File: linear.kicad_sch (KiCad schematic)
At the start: 8 parts, among them J5 VSENSE, U7 LT3045xDD

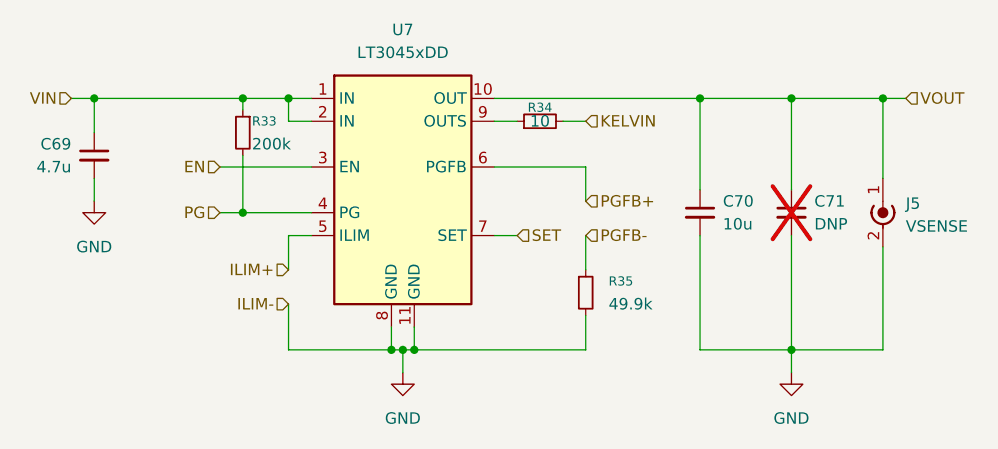
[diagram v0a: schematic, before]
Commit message: reorg and add 10MHz
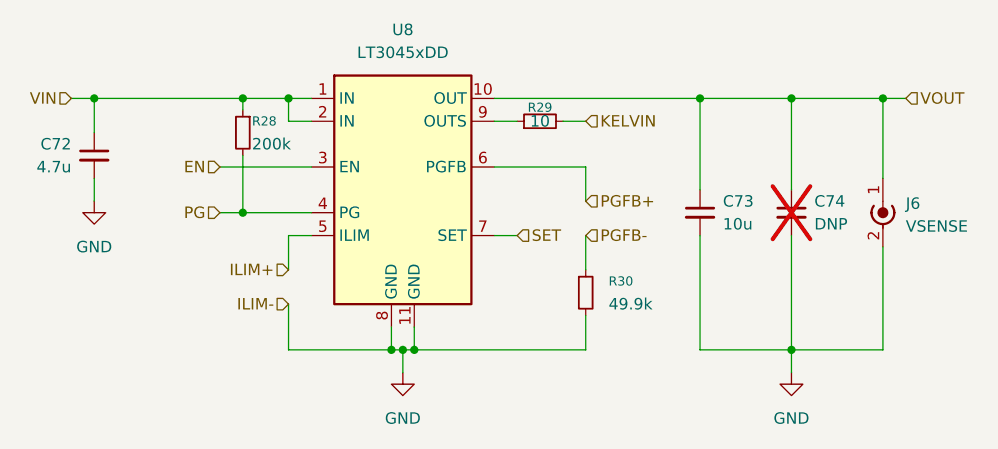
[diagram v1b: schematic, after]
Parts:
- renumbered C69 to C72, C70 to C73, C71 to C74, J5 to J6, R33 to R28, R34 to R29, R35 to R30, U7 to U8

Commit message: Renumber refdes
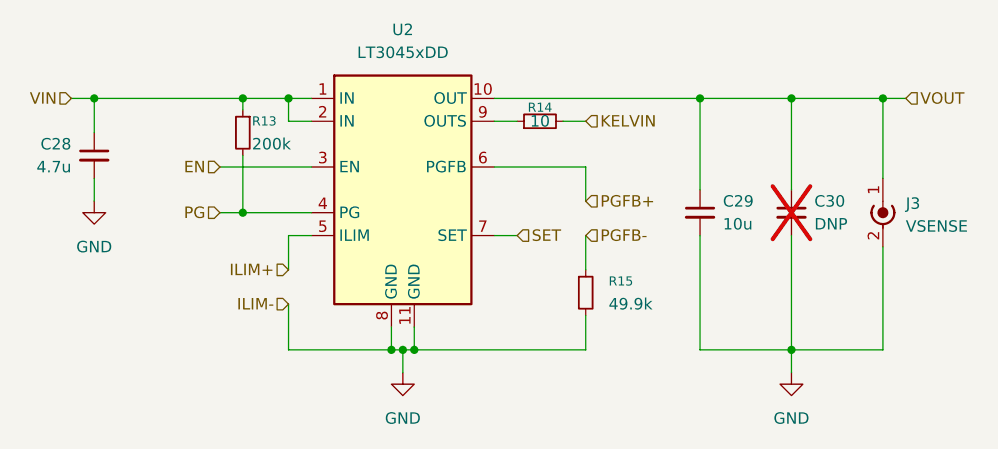
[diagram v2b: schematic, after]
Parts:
- renumbered C72 to C28, C73 to C29, C74 to C30, J6 to J3, R28 to R13, R29 to R14, R30 to R15, U8 to U2
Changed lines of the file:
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@@
 		(dnp yes)
 		(fields_autoplaced yes)
-		(property "Reference" "C74"
+		(property "Reference" "C30"
 			(at 142.24 92.7162 0)
 			(effects
@@
 			(project "huskypointofload"
 				(path "/eb9c972b-d134-41da-be97-ece3f463f7e0/28dccbc8-62a2-4750-b12f-4e220cef19bd/1008e2fb-3ddd-4ae6-bc4d-94ec83ca7d40"
-					(reference "C74")
+					(reference "C30")
 					(unit 1)
 				)
@@
 				)
 				(path "/eb9c972b-d134-41da-be97-ece3f463f7e0/28dccbc8-62a2-4750-b12f-4e220cef19bd/94144f86-6c10-4bf6-8112-48c8c30ee72b"
-					(reference "C71")
+					(reference "C47")
 					(unit 1)
 				)
@@
 		(dnp no)
 		(fields_autoplaced yes)
-		(property "Reference" "#PWR068"
+		(property "Reference" "#PWR034"
 			(at 62.23 99.06 0)
 			(effects
@@
 			(project "huskypointofload"
 				(path "/eb9c972b-d134-41da-be97-ece3f463f7e0/28dccbc8-62a2-4750-b12f-4e220cef19bd/1008e2fb-3ddd-4ae6-bc4d-94ec83ca7d40"
-					(reference "#PWR068")
-					(unit 1)
-				)
-				(path "/eb9c972b-d134-41da-be97-ece3f463f7e0/28dccbc8-62a2-4750-b12f-4e220cef19bd/89c1d7e3-bbee-4284-843e-668e09d75bda"
-					(reference "#PWR076")
-					(unit 1)
-				)
-				(path "/eb9c972b-d134-41da-be97-ece3f463f7e0/28dccbc8-62a2-4750-b12f-4e220cef19bd/94144f86-6c10-4bf6-8112-48c8c30ee72b"
-					(reference "#PWR065")
+					(reference "#PWR034")
+					(unit 1)
+				)
+				(path "/eb9c972b-d134-41da-be97-ece3f463f7e0/28dccbc8-62a2-4750-b12f-4e220cef19bd/89c1d7e3-bbee-4284-843e-668e09d75bda"
+					(reference "#PWR0136")
+					(unit 1)
+				)
+				(path "/eb9c972b-d134-41da-be97-ece3f463f7e0/28dccbc8-62a2-4750-b12f-4e220cef19bd/94144f86-6c10-4bf6-8112-48c8c30ee72b"
+					(reference "#PWR039")
 					(unit 1)
 				)
@@
 		(dnp no)
 		(fields_autoplaced yes)
-		(property "Reference" "U8"
+		(property "Reference" "U2"
 			(at 96.52 73.66 0)
 			(effects
@@
 			(project "huskypointofload"
 				(path "/eb9c972b-d134-41da-be97-ece3f463f7e0/28dccbc8-62a2-4750-b12f-4e220cef19bd/1008e2fb-3ddd-4ae6-bc4d-94ec83ca7d40"
-					(reference "U8")
+					(reference "U2")
 					(unit 1)
 				)
@@
 				)
 				(path "/eb9c972b-d134-41da-be97-ece3f463f7e0/28dccbc8-62a2-4750-b12f-4e220cef19bd/94144f86-6c10-4bf6-8112-48c8c30ee72b"
-					(reference "U7")
+					(reference "U5")
 					(unit 1)
 				)
@@
 		(on_board yes)
 		(dnp no)
-		(property "Reference" "C72"
+		(property "Reference" "C28"
 			(at 59.69 86.3662 0)
 			(effects
@@
 			(project "huskypointofload"
 				(path "/eb9c972b-d134-41da-be97-ece3f463f7e0/28dccbc8-62a2-4750-b12f-4e220cef19bd/1008e2fb-3ddd-4ae6-bc4d-94ec83ca7d40"
-					(reference "C72")
+					(reference "C28")
 					(unit 1)
 				)
@@
 				)
 				(path "/eb9c972b-d134-41da-be97-ece3f463f7e0/28dccbc8-62a2-4750-b12f-4e220cef19bd/94144f86-6c10-4bf6-8112-48c8c30ee72b"
-					(reference "C69")
+					(reference "C45")
 					(unit 1)
 				)
@@
 		(dnp no)
 		(fields_autoplaced yes)
-		(property "Reference" "J6"
+		(property "Reference" "J3"
 			(at 152.4 92.9639 0)
 			(effects
@@
 			(project "huskypointofload"
 				(path "/eb9c972b-d134-41da-be97-ece3f463f7e0/28dccbc8-62a2-4750-b12f-4e220cef19bd/1008e2fb-3ddd-4ae6-bc4d-94ec83ca7d40"
-					(reference "J6")
+					(reference "J3")
 					(unit 1)
 				)
@@
 				)
 				(path "/eb9c972b-d134-41da-be97-ece3f463f7e0/28dccbc8-62a2-4750-b12f-4e220cef19bd/94144f86-6c10-4bf6-8112-48c8c30ee72b"
-					(reference "J5")
+					(reference "J4")
 					(unit 1)
 				)
@@
 		(dnp no)
 		(fields_autoplaced yes)
-		(property "Reference" "#PWR070"
+		(property "Reference" "#PWR036"
 			(at 139.7 118.11 0)
 			(effects
@@
 			(project "huskypointofload"
 				(path "/eb9c972b-d134-41da-be97-ece3f463f7e0/28dccbc8-62a2-4750-b12f-4e220cef19bd/1008e2fb-3ddd-4ae6-bc4d-94ec83ca7d40"
-					(reference "#PWR070")
-					(unit 1)
-				)
-				(path "/eb9c972b-d134-41da-be97-ece3f463f7e0/28dccbc8-62a2-4750-b12f-4e220cef19bd/89c1d7e3-bbee-4284-843e-668e09d75bda"
-					(reference "#PWR078")
-					(unit 1)
-				)
-				(path "/eb9c972b-d134-41da-be97-ece3f463f7e0/28dccbc8-62a2-4750-b12f-4e220cef19bd/94144f86-6c10-4bf6-8112-48c8c30ee72b"
-					(reference "#PWR067")
+					(reference "#PWR036")
+					(unit 1)
+				)
+				(path "/eb9c972b-d134-41da-be97-ece3f463f7e0/28dccbc8-62a2-4750-b12f-4e220cef19bd/89c1d7e3-bbee-4284-843e-668e09d75bda"
+					(reference "#PWR0138")
+					(unit 1)
+				)
+				(path "/eb9c972b-d134-41da-be97-ece3f463f7e0/28dccbc8-62a2-4750-b12f-4e220cef19bd/94144f86-6c10-4bf6-8112-48c8c30ee72b"
+					(reference "#PWR041")
 					(unit 1)
 				)
@@
 		(dnp no)
 		(fields_autoplaced yes)
-		(property "Reference" "C73"
+		(property "Reference" "C29"
 			(at 132.08 92.7162 0)
 			(effects
@@
 			(project "huskypointofload"
 				(path "/eb9c972b-d134-41da-be97-ece3f463f7e0/28dccbc8-62a2-4750-b12f-4e220cef19bd/1008e2fb-3ddd-4ae6-bc4d-94ec83ca7d40"
-					(reference "C73")
+					(reference "C29")
 					(unit 1)
 				)
@@
 				)
 				(path "/eb9c972b-d134-41da-be97-ece3f463f7e0/28dccbc8-62a2-4750-b12f-4e220cef19bd/94144f86-6c10-4bf6-8112-48c8c30ee72b"
-					(reference "C70")
+					(reference "C46")
 					(unit 1)
 				)
@@
 		(on_board yes)
 		(dnp no)
-		(property "Reference" "R29"
+		(property "Reference" "R14"
 			(at 111.76 82.296 90)
 			(effects
@@
 			(project "huskypointofload"
 				(path "/eb9c972b-d134-41da-be97-ece3f463f7e0/28dccbc8-62a2-4750-b12f-4e220cef19bd/1008e2fb-3ddd-4ae6-bc4d-94ec83ca7d40"
-					(reference "R29")
-					(unit 1)
-				)
-				(path "/eb9c972b-d134-41da-be97-ece3f463f7e0/28dccbc8-62a2-4750-b12f-4e220cef19bd/89c1d7e3-bbee-4284-843e-668e09d75bda"
-					(reference "R34")
-					(unit 1)
-				)
-				(path "/eb9c972b-d134-41da-be97-ece3f463f7e0/28dccbc8-62a2-4750-b12f-4e220cef19bd/94144f86-6c10-4bf6-8112-48c8c30ee72b"
-					(reference "R26")
+					(reference "R14")
+					(unit 1)
+				)
+				(path "/eb9c972b-d134-41da-be97-ece3f463f7e0/28dccbc8-62a2-4750-b12f-4e220cef19bd/89c1d7e3-bbee-4284-843e-668e09d75bda"
+					(reference "R89")
+					(unit 1)
+				)
+				(path "/eb9c972b-d134-41da-be97-ece3f463f7e0/28dccbc8-62a2-4750-b12f-4e220cef19bd/94144f86-6c10-4bf6-8112-48c8c30ee72b"
+					(reference "R19")
 					(unit 1)
 				)
@@
 		(on_board yes)
 		(dnp no)
-		(property "Reference" "R28"
+		(property "Reference" "R13"
 			(at 79.756 83.82 0)
 			(effects
@@
 			(project "huskypointofload"
 				(path "/eb9c972b-d134-41da-be97-ece3f463f7e0/28dccbc8-62a2-4750-b12f-4e220cef19bd/1008e2fb-3ddd-4ae6-bc4d-94ec83ca7d40"
-					(reference "R28")
-					(unit 1)
-				)
-				(path "/eb9c972b-d134-41da-be97-ece3f463f7e0/28dccbc8-62a2-4750-b12f-4e220cef19bd/89c1d7e3-bbee-4284-843e-668e09d75bda"
-					(reference "R33")
-					(unit 1)
-				)
-				(path "/eb9c972b-d134-41da-be97-ece3f463f7e0/28dccbc8-62a2-4750-b12f-4e220cef19bd/94144f86-6c10-4bf6-8112-48c8c30ee72b"
-					(reference "R25")
+					(reference "R13")
+					(unit 1)
+				)
+				(path "/eb9c972b-d134-41da-be97-ece3f463f7e0/28dccbc8-62a2-4750-b12f-4e220cef19bd/89c1d7e3-bbee-4284-843e-668e09d75bda"
+					(reference "R88")
+					(unit 1)
+				)
+				(path "/eb9c972b-d134-41da-be97-ece3f463f7e0/28dccbc8-62a2-4750-b12f-4e220cef19bd/94144f86-6c10-4bf6-8112-48c8c30ee72b"
+					(reference "R18")
 					(unit 1)
 				)
@@
 		(on_board yes)
 		(dnp no)
-		(property "Reference" "R30"
+		(property "Reference" "R15"
 			(at 119.38 101.5999 0)
 			(effects
@@
 			(project "huskypointofload"
 				(path "/eb9c972b-d134-41da-be97-ece3f463f7e0/28dccbc8-62a2-4750-b12f-4e220cef19bd/1008e2fb-3ddd-4ae6-bc4d-94ec83ca7d40"
-					(reference "R30")
-					(unit 1)
-				)
-				(path "/eb9c972b-d134-41da-be97-ece3f463f7e0/28dccbc8-62a2-4750-b12f-4e220cef19bd/89c1d7e3-bbee-4284-843e-668e09d75bda"
-					(reference "R35")
-					(unit 1)
-				)
-				(path "/eb9c972b-d134-41da-be97-ece3f463f7e0/28dccbc8-62a2-4750-b12f-4e220cef19bd/94144f86-6c10-4bf6-8112-48c8c30ee72b"
-					(reference "R27")
+					(reference "R15")
+					(unit 1)
+				)
+				(path "/eb9c972b-d134-41da-be97-ece3f463f7e0/28dccbc8-62a2-4750-b12f-4e220cef19bd/89c1d7e3-bbee-4284-843e-668e09d75bda"
+					(reference "R90")
+					(unit 1)
+				)
+				(path "/eb9c972b-d134-41da-be97-ece3f463f7e0/28dccbc8-62a2-4750-b12f-4e220cef19bd/94144f86-6c10-4bf6-8112-48c8c30ee72b"
+					(reference "R20")
 					(unit 1)
 				)
@@
 		(dnp no)
 		(fields_autoplaced yes)
-		(property "Reference" "#PWR069"
+		(property "Reference" "#PWR035"
 			(at 96.52 118.11 0)
 			(effects
@@
 			(project "huskypointofload"
 				(path "/eb9c972b-d134-41da-be97-ece3f463f7e0/28dccbc8-62a2-4750-b12f-4e220cef19bd/1008e2fb-3ddd-4ae6-bc4d-94ec83ca7d40"
-					(reference "#PWR069")
-					(unit 1)
-				)
-				(path "/eb9c972b-d134-41da-be97-ece3f463f7e0/28dccbc8-62a2-4750-b12f-4e220cef19bd/89c1d7e3-bbee-4284-843e-668e09d75bda"
-					(reference "#PWR077")
-					(unit 1)
-				)
-				(path "/eb9c972b-d134-41da-be97-ece3f463f7e0/28dccbc8-62a2-4750-b12f-4e220cef19bd/94144f86-6c10-4bf6-8112-48c8c30ee72b"
-					(reference "#PWR066")
-					(unit 1)
-				)
+					(reference "#PWR035")
+					(unit 1)
+				)
+				(path "/eb9c972b-d134-41da-be97-ece3f463f7e0/28dccbc8-62a2-4750-b12f-4e220cef19bd/89c1d7e3-bbee-4284-843e-668e09d75bda"
+					(reference "#PWR0137")
+					(unit 1)
+				)
+				(path "/eb9c972b-d134-41da-be97-ece3f463f7e0/28dccbc8-62a2-4750-b12f-4e220cef19bd/94144f86-6c10-4bf6-8112-48c8c30ee72b"
+					(reference "#PWR040")
+					(unit 1)
+				)
